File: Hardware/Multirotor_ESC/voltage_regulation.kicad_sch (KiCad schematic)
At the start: 18 parts

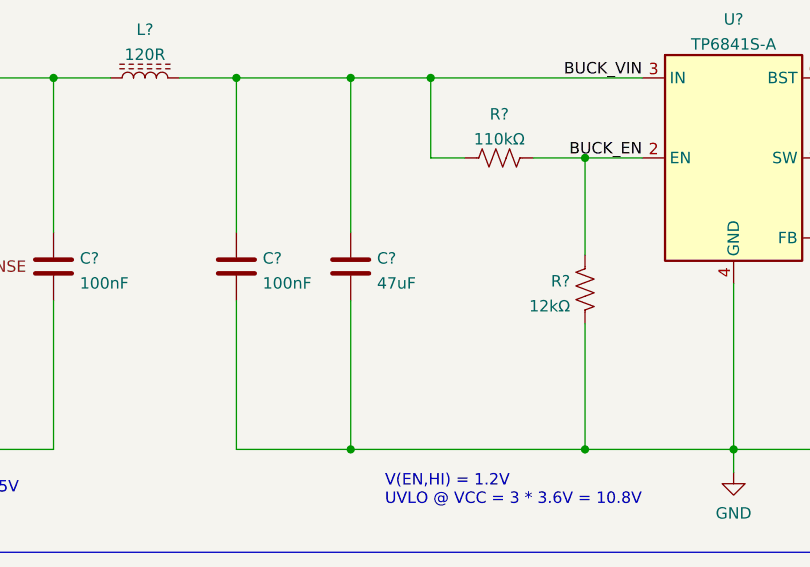
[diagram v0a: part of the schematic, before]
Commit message: Added Phase Half-Bridge Circuit
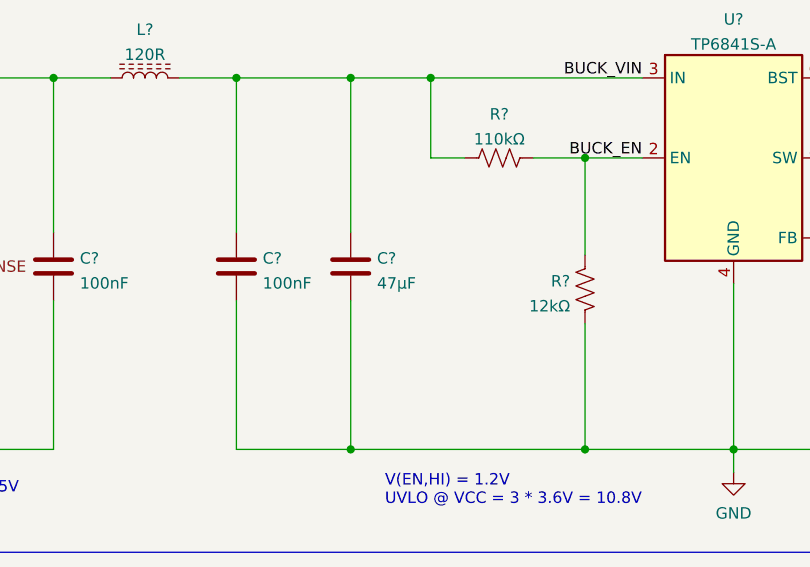
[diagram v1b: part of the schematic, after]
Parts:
- C?: value 47uF -> 47μF
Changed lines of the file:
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@@
       (effects (font (size 1.27 1.27)) (justify left))
     )
-    (property "Value" "47uF" (id 1) (at 133.731 75.5266 0)
+    (property "Value" "47μF" (id 1) (at 133.731 75.5266 0)
       (effects (font (size 1.27 1.27)) (justify left))
     )
